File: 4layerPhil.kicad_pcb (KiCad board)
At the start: 4 copper layers, 71 x 56 mm, 52 parts, among them J1 USB_B_Micro, J2 Conn_01x05_Pin, J3 Conn_01x04_Pin, J5 Conn_01x05_Pin, J6 1140084168, SW1 SW_SPDT, SW2 BTN1, SW3 BTN2, SW4 BTN3, U1 AMS1117-3.3, U2 USBLC6-2P6, U3 STM32F103RCTx, Y1 16MHz

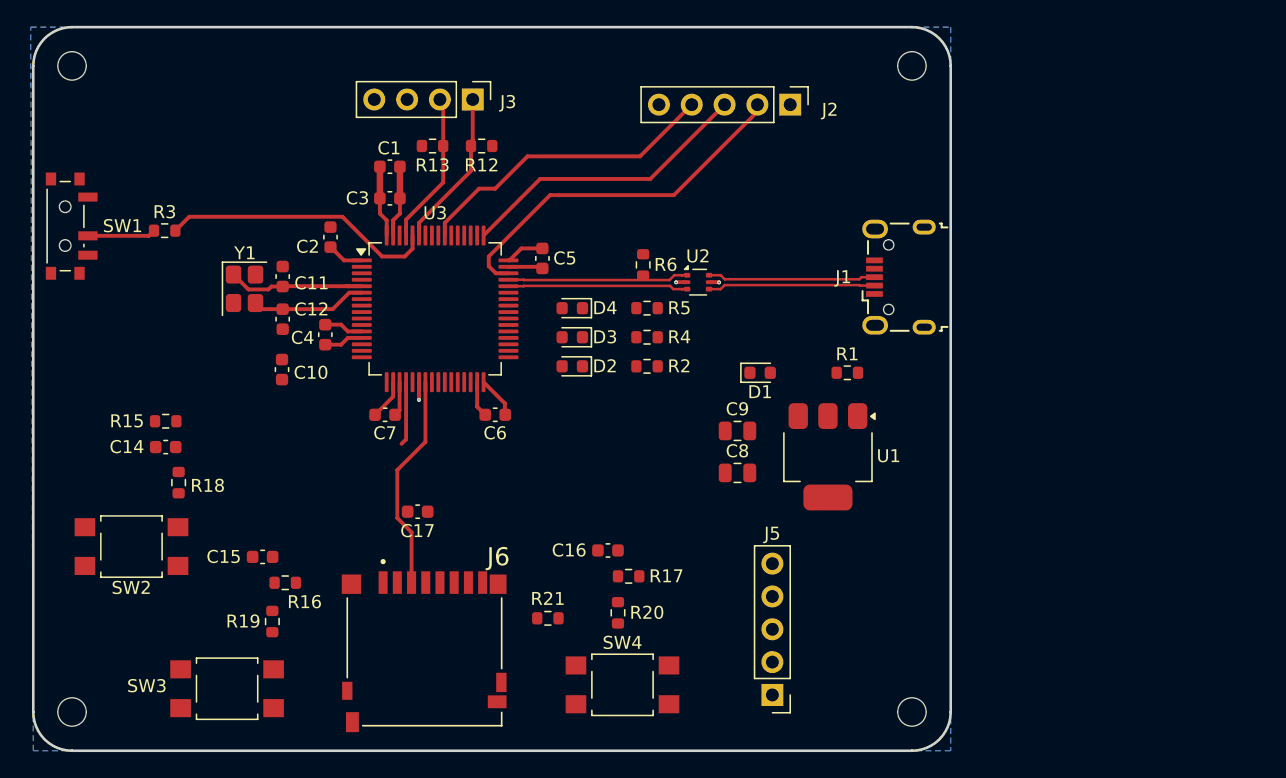
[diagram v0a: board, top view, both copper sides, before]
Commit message: completed all signal routes, switched btn placemenets
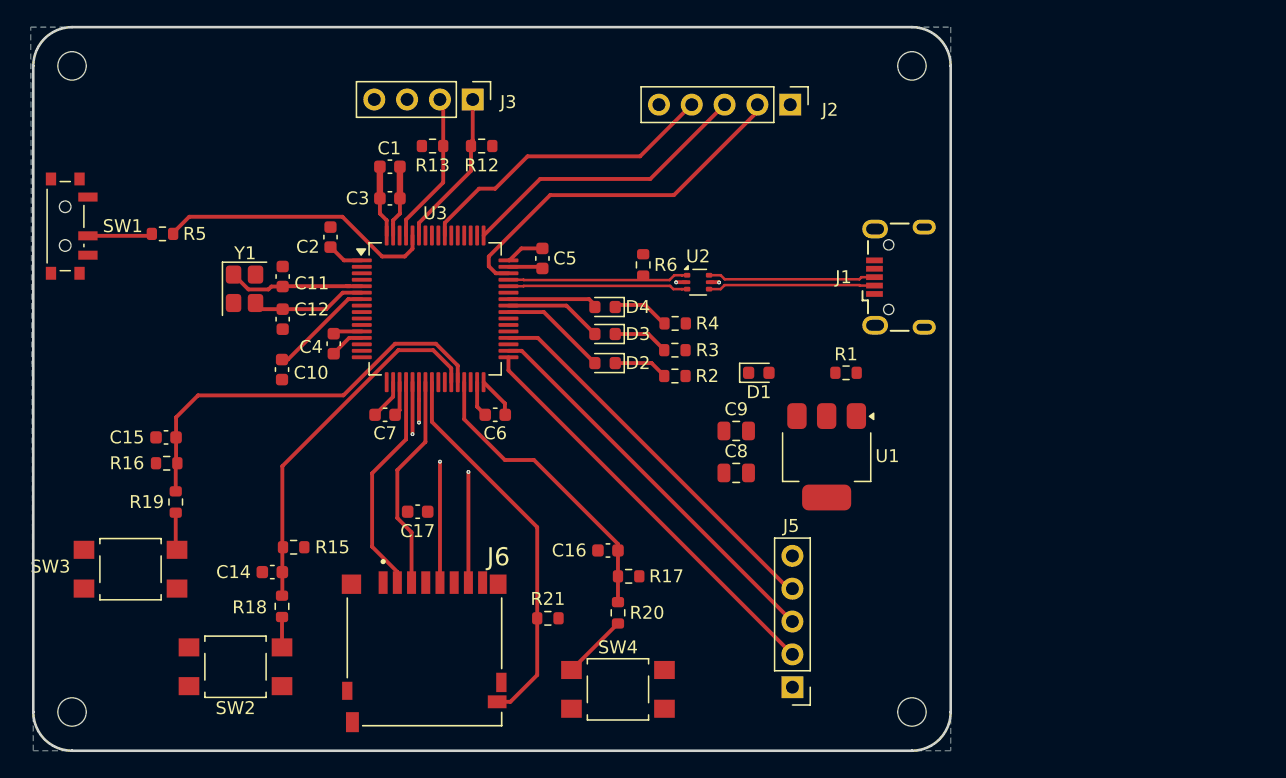
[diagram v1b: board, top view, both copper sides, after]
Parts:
- R3: value 10k -> 500
- R4: value 500 -> 1k
- R5: value 1k -> 10k
- moved R3 40.6 mm to (156.7, 77.0)
- moved R5 37.9 mm to (117.0, 68.0)
- moved R15 13.9 mm to (127.2, 92.2), turned to 0 degrees
- moved R16 13.0 mm to (117.3, 85.8), turned to 180 degrees
- moved C14 12.7 mm to (125.5, 94.2)
- moved R18 12.5 mm to (126.2, 96.8), turned to -90 degrees
- moved SW2 12.3 mm to (122.7, 101.5)
- moved C15 11.9 mm to (117.3, 83.8)
- moved R19 11.9 mm to (118.0, 88.8)
- moved SW3 11.9 mm to (114.5, 94.0)
- moved D2 2.55 mm to (151.2, 78.0)
- moved D3 2.55 mm to (151.2, 75.8)
- moved D4 2.54 mm to (151.2, 73.7)
- moved R4 2.42 mm to (156.7, 74.9)
- moved R2 2.28 mm to (156.7, 79.0)
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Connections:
- R3 pad 1: /SW_BOOT0 -> /USR_LED_BLU_K
- R3 pad 2: /BOOT0 -> GND
- R4 pad 1: /USR_LED_BLU_K -> /USR_LED_GRN_K
- R5 pad 1: /USR_LED_GRN_K -> /SW_BOOT0
- R5 pad 2: GND -> /BOOT0
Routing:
- net /I2S2_WS: track 0.00 -> 32.1 mm
- net USR_BTN_2: track 0.00 -> 32.0 mm
- net /I2S2_CK: track 0.00 -> 30.7 mm
- net /I2S2_SD: track 0.00 -> 30.0 mm
- net MICROSD_DETB: track 0.00 -> 30.0 mm
- net USR_BTN_1: track 0.00 -> 28.5 mm
- net USR_BTN_3: track 0.00 -> 23.3 mm
- net SPI_SCK: track 0.00 -> 16.4 mm, vias 0 -> 2
- net SPI_MISO: track 1.38 -> 17.1 mm, vias 1 -> 2
- net SPI_NSS: track 4.92 -> 17.4 mm
- net /USR_LED_RED: track 0.00 -> 8.32 mm
- net /NRST: track 0.00 -> 8.11 mm
- net /USR_LED_BLU: track 0.00 -> 7.60 mm
- net /USR_LED_GRN: track 0.00 -> 6.87 mm
- net /USR_BTN_3R: track 0.00 -> 5.09 mm
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
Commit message: added routes and viases
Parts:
- moved C17 1.80 mm to (137.3, 91.2), turned to -90 degrees
- moved C6 0.61 mm to (142.4, 81.5)
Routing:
- net USR_BTN_1: track 28.5 -> 11.6 mm, vias 0 -> 1
- net SPI_SCK: track 16.4 -> 7.55 mm
- net GND: track 17.1 -> 21.4 mm, vias 1 -> 4
- net VBUS: track 1.59 -> 3.63 mm, vias 1 -> 2
- net +3V3: track 20.0 -> 19.4 mm

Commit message: different GND layer, started power supply section
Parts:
- moved C8 11.8 mm to (164.9, 75.2)
- moved D1 9.92 mm to (172.9, 80.6), turned to -90 degrees
- moved C9 9.00 mm to (169.9, 80.5), turned to 90 degrees
- moved U1 5.67 mm to (164.9, 80.8)
- moved R1 3.75 mm to (173.6, 78.0)
- moved R5 1.82 mm to (117.5, 66.2)
- moved R16 1.50 mm to (118.8, 85.8), turned to 0 degrees
- moved C17 0.92 mm to (137.3, 90.3)
- moved C5 0.73 mm to (146.2, 69.2)
- moved SW1 0.65 mm to (109.8, 66.8)
- moved R4 0.07 mm to (156.7, 75.0)
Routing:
- net +3V3: track 19.4 -> 191.1 mm, vias 0 -> 15
- net GND: track 21.4 -> 60.2 mm, vias 4 -> 30
- net USR_BTN_1: track 11.6 -> 26.1 mm, vias 1 -> 2
- net SPI_SCK: track 7.55 -> 16.4 mm
- net /SWDIO: track 28.7 -> 24.7 mm
- net SPI_NSS: track 16.9 -> 15.8 mm
- net /SW_BOOT0: track 5.28 -> 5.94 mm
- net /BOOT0: track 21.7 -> 21.1 mm
- added copper zone on F.Cu, net +3V3
- added copper zone on F.Cu, net GND
- added copper zone on In1.Cu, net GND
- added copper zone on F.Cu, net VBUS
- removed copper zone on B.Cu, net GND

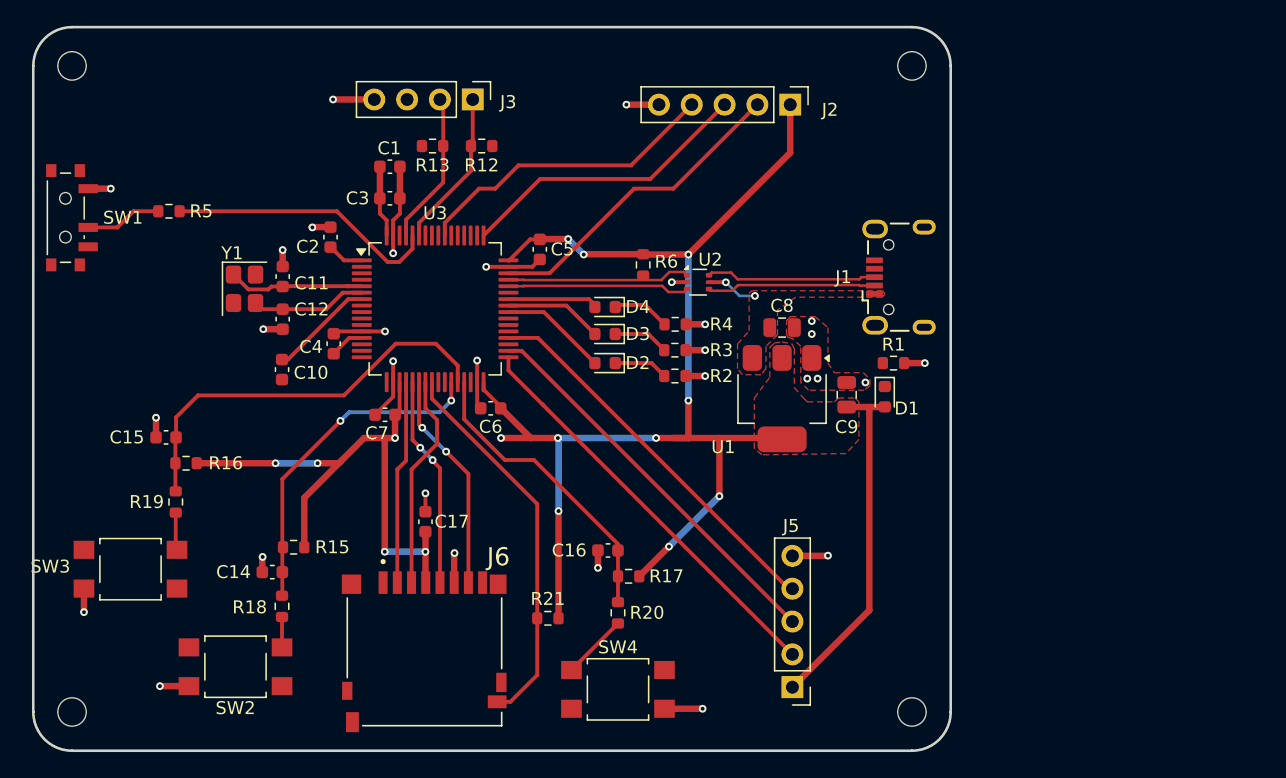
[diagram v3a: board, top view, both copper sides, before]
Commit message: Preparation for changing LDO to impulse regulator, SWDIO to a correct connector etc.
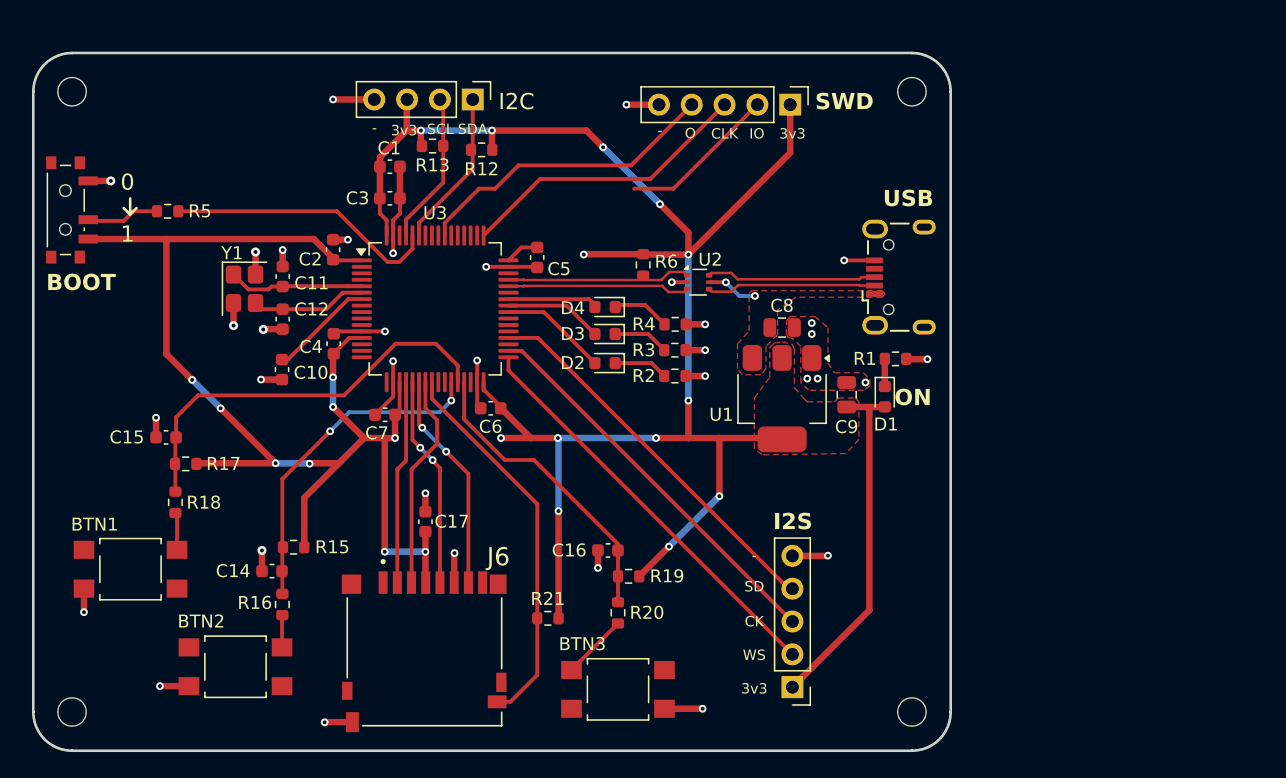
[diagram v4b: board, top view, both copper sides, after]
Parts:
- R16: value 10k -> 1k5
- R19: value 1k5 -> 10k
- moved R19 35.5 mm to (153.1, 94.5), turned to 0 degrees
- moved R17 35.4 mm to (118.8, 85.8)
- moved R16 13.2 mm to (126.3, 96.7), turned to -90 degrees
- moved R18 11.5 mm to (118.0, 88.8)
- moved H1 2.00 mm to (175.0, 57.0)
- moved H4 2.00 mm to (110.0, 57.0)
- moved C2 1.00 mm to (130.2, 69.2)
- moved C5 0.66 mm to (146.0, 69.8)
- moved SW1 0.60 mm to (109.8, 66.2)
- moved R1 0.36 mm to (173.7, 77.7)
- moved R12 0.30 mm to (141.7, 61.5)
- moved R5 0.10 mm to (117.4, 66.2)
- moved C14 0.08 mm to (125.5, 94.1)
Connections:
- R16 pad 1: USR_BTN_2 -> USR_BTN_1
- R16 pad 2: +3V3 -> /USR_BTN_1R
- R17 pad 1: USR_BTN_3 -> USR_BTN_2
- R18 pad 1: USR_BTN_1 -> USR_BTN_2
- R18 pad 2: /USR_BTN_1R -> /USR_BTN_2R
- R19 pad 1: USR_BTN_2 -> USR_BTN_3
- R19 pad 2: /USR_BTN_2R -> +3V3
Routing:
- net +3V3: track 191.1 -> 268.7 mm, vias 15 -> 22
- net /SWDIO: track 24.7 -> 12.2 mm
- net GND: track 60.2 -> 69.5 mm, vias 30 -> 35
- net /PWR_LED_K: track 0.00 -> 2.14 mm
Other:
- board size 71 x 56 mm -> 71 x 54 mm
- board text added: "-"
- board text added: "0"
- board text added: "09/26 V0.1"
- board text added: "1"
- board text added: "3v3"
- board text added: "BOOT"
- board text added: "BTN1"
- board text added: "BTN2"
- board text added: "BTN3"
- board text added: "CK"
- board text added: "CLK"
- board text added: "I2C"
- board text added: "I2S"
- board text added: "IO"
- board text added: "O"
- board text added: "ON"
- board text added: "SCL"
- board text added: "SD"
- board text added: "SDA"
- board text added: "SWD"
- board text added: "USB"
- board text added: "WS"

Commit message: Added gain
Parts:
- added R22: 100k, Resistor_SMD:R_0603_1608Metric, F.Cu at (169.6, 92.0)
- added R23: 100k, Resistor_SMD:R_0603_1608Metric, F.Cu at (169.8, 94.6)
- J5: value Conn_01x05_Pin -> Conn_01x06_Pin; footprint Connector_PinHeader_2.54mm:PinHeader_1x05_P2.54mm_Vertical -> Connector_PinHeader_2.54mm:PinHeader_1x06_P2.54mm_Vertical
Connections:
- J5 pad 5: GND -> /I2S2_GAIN
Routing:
- net /I2S2_GAIN: track 0.00 -> 6.43 mm
- net GND: track 69.5 -> 71.4 mm, vias 35 -> 36
- net +3V3: track 268.7 -> 270.0 mm
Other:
- board text added: "GAIN"

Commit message: assigned VBUS and GND as power lines for type-c receptacle schematic
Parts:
- J1: value USB_B_Micro -> USB_C_Receptacle_USB2.0_16P; footprint Connector_USB:USB_Micro-B_Wuerth_629105150521 -> Connector_USB:USB_C_Receptacle_GCT_USB4110
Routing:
- net unconnected-(J1-SBU1-PadA8): track 0.00 -> 2.35 mm, vias 0 -> 1
- net GND: track 71.4 -> 69.1 mm, vias 36 -> 35

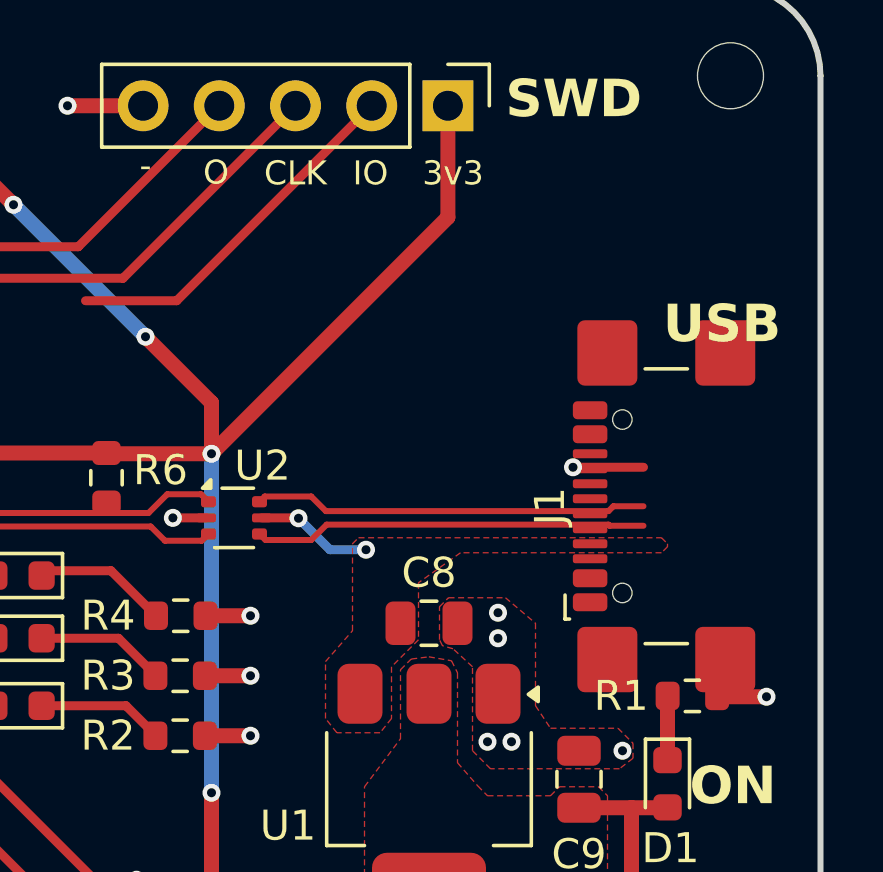
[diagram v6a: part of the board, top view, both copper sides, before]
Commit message: Switched from MicroB to USB Type-C and smaller changes
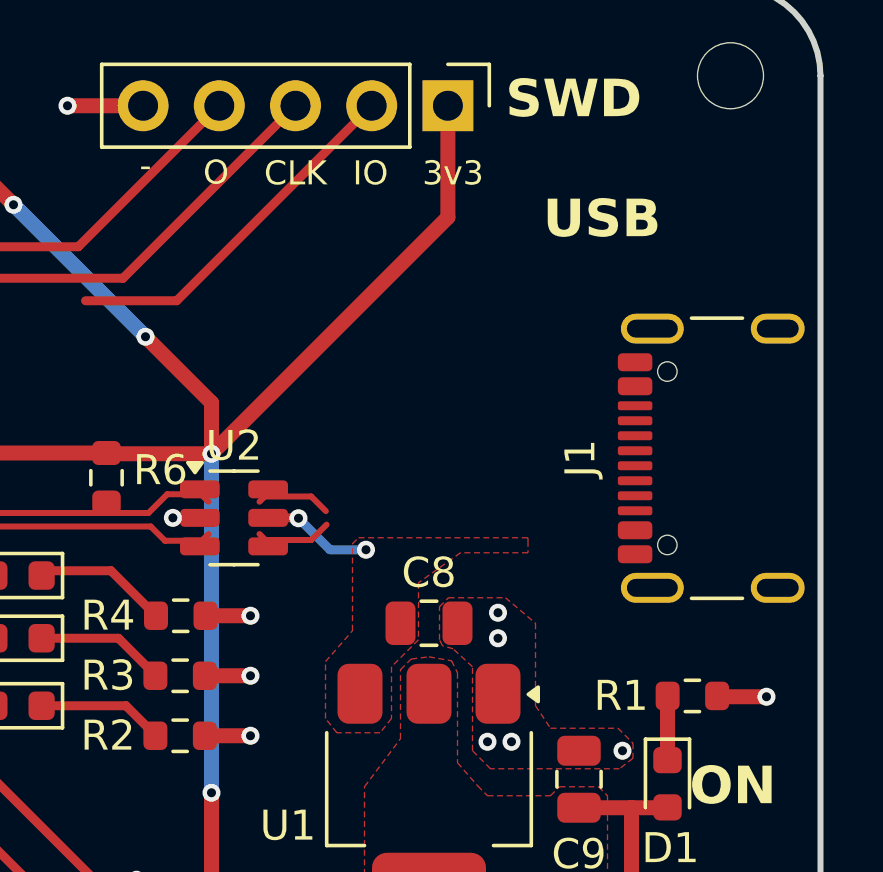
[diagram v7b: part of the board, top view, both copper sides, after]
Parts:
- J1: footprint Connector_USB:USB_C_Receptacle_GCT_USB4110 -> Connector_USB:USB_C_Receptacle_GCT_USB4105-xx-A_16P_TopMnt_Horizontal
- U2: value USBLC6-2P6 -> USBLC6-2SC6; footprint Package_TO_SOT_SMD:SOT-666 -> Package_TO_SOT_SMD:SOT-23-6
- moved J1 2.19 mm to (175.5, 69.8)
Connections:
- J1 pad S1: unconnected-(J1-SHIELD-PadS1) -> GND
- U2 pad 1: /USB_D+ -> /USB_D-
- U2 pad 3: /USB_D- -> /USB_D+
- U2 pad 4: /D_USB- -> /D_USB+
- U2 pad 6: /D_USB+ -> /D_USB-
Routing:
- net /D_USB-: track 13.1 -> 2.49 mm
- net /D_USB+: track 13.1 -> 2.53 mm
- net unconnected-(J1-SBU1-PadA8): track 2.35 -> 0.00 mm, vias 1 -> 0
